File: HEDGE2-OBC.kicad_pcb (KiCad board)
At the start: 4 copper layers, 90.2 x 95.9 mm, 55 parts, among them J1 SQT-110-01-L-D, J2 MMBX-S50-0-18, J3 SMA-J-P-X-RA-TH1, U1 OEM719, U2 INA260AIPWR, U3 TCAN1046AVDYYRQ1, U4 INA260AIPWR, U5 TPS543320RPYR

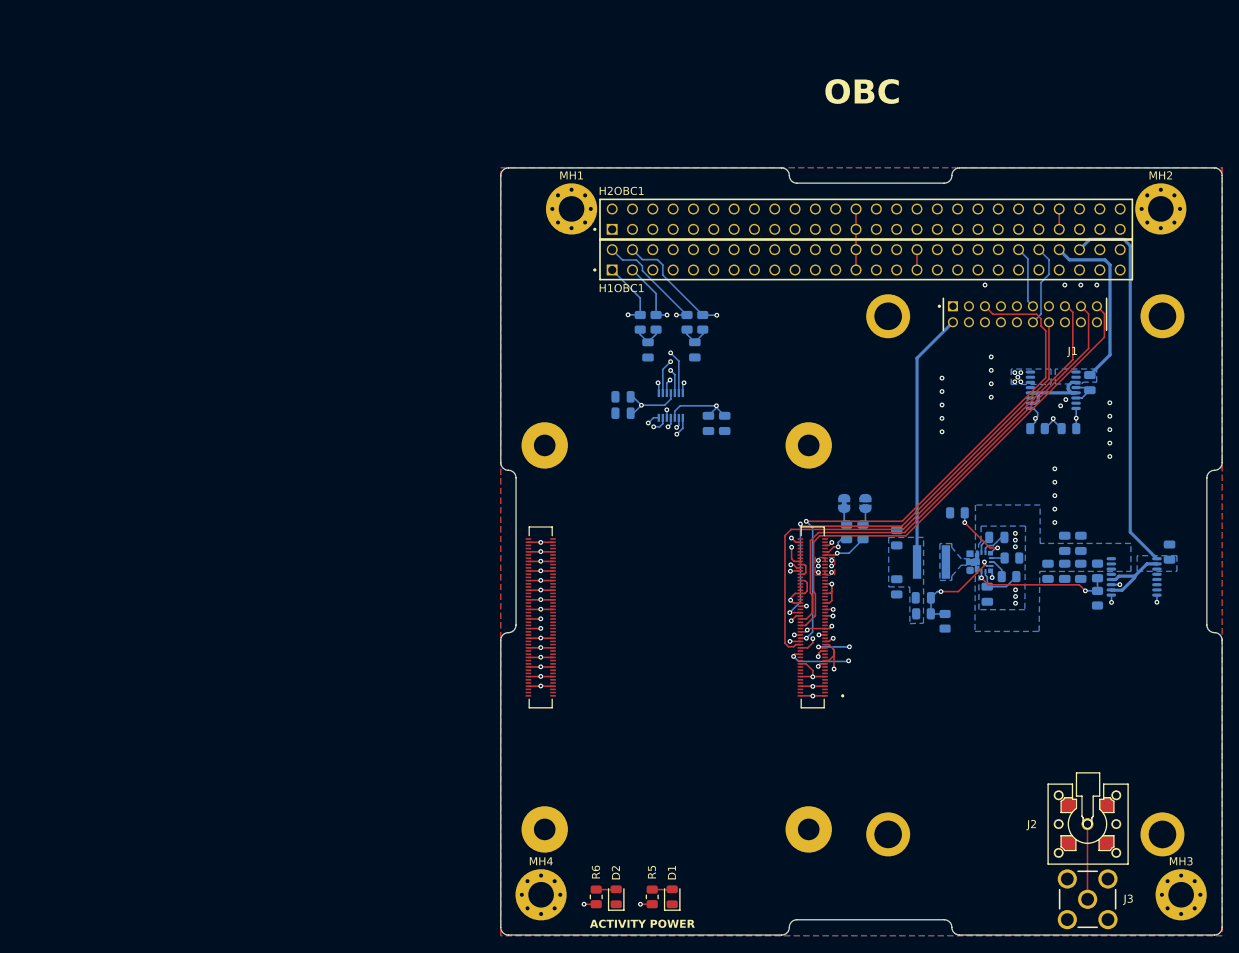
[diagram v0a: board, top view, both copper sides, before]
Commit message: Start new PCB layout for second test article
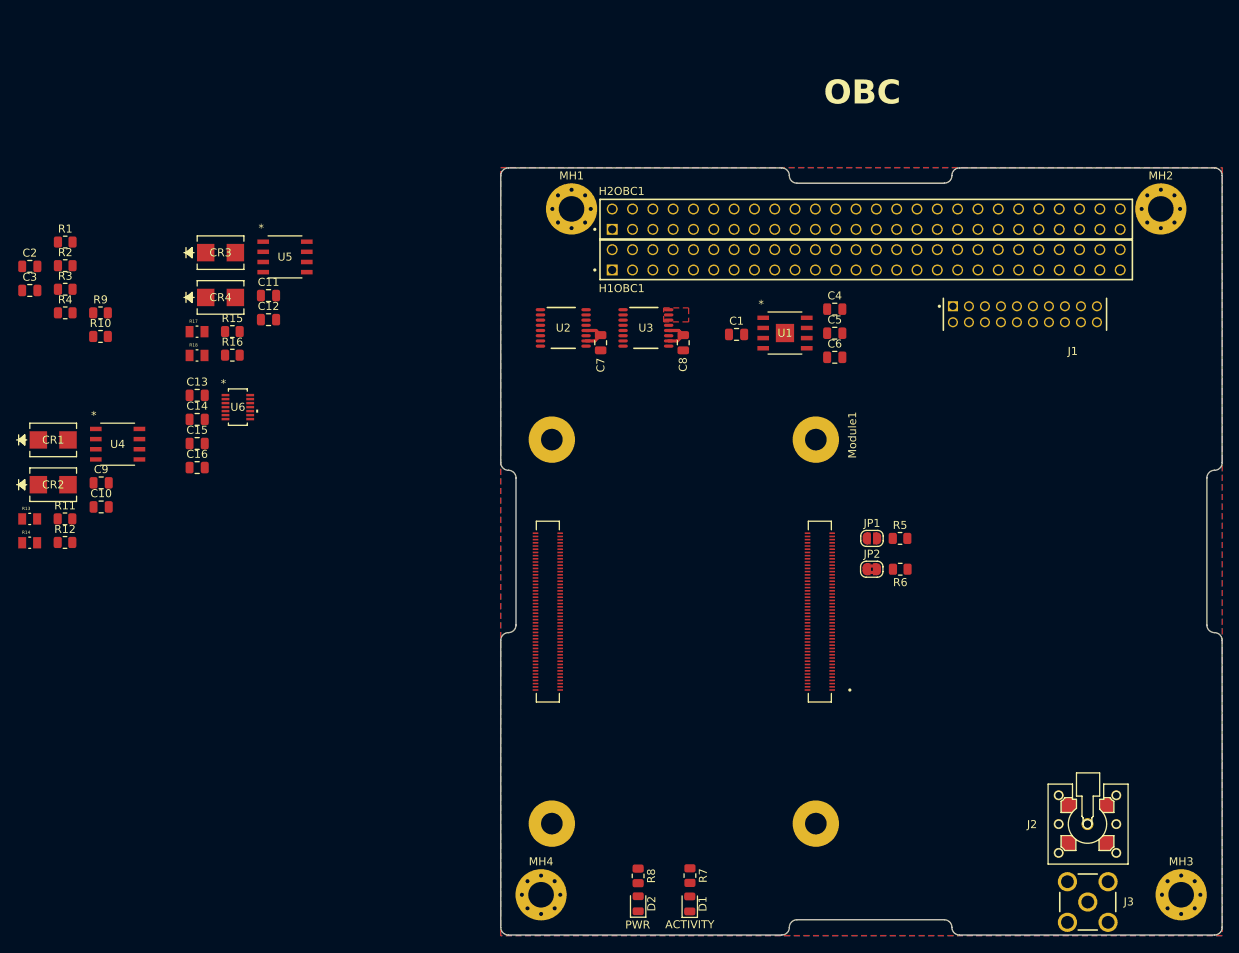
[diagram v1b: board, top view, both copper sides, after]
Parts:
- removed C17, C18: 47u, 10V, 0805, Capacitor_SMD:C_0805_2012Metric
- removed L1: XGL5050-182MEC, XGL5050-182MEC:IND_XGL5050_COC
- added CR1: SMBJ43CA, SMBJ43CA:SMBJSeries_LTF, F.Cu at (108.2, 123.5)
- added CR2: SMBJ43CA, SMBJ43CA:SMBJSeries_LTF, F.Cu at (108.2, 129.1)
- added CR3: SMBJ43CA, SMBJ43CA:SMBJSeries_LTF, F.Cu at (129.1, 100.1)
- added CR4: SMBJ43CA, SMBJ43CA:SMBJSeries_LTF, F.Cu at (129.1, 105.7)
- added R18: CRGP0805F10R, CRGP0805F10R:RESC2012X65N, F.Cu at (126.1, 113.0)
- added U6: TCAN1046AVDYYRQ1, TCAN1046AV:SOT23_DYY_TEX, F.Cu at (131.2, 119.4)
- C1, C5: value 0u1 -> 1u; moved to F.Cu
- C10, C11: value 10u, 25V, 0805 -> 100n; moved to F.Cu
- C12: value 0u1, 50v, 0805 -> 100n; moved to F.Cu
- C13: value 0u1, 50v, 0805 -> 4u7; moved to F.Cu
- C14: value 2u2, 10V, 0805 -> 0u1; moved to F.Cu
- C15: value 0u1, 50V, 0805 -> 4u7; moved to F.Cu
- C16: value 33p -> 0u1; moved to F.Cu
- C2, C8, JP1, R1, R10, R15, R2, R3, R4, R9, U2: moved to F.Cu
- C3: value 0.1u -> 0u1; moved to F.Cu
- C4: value 4u7 -> 10u; moved to F.Cu
- C6: value 4u7 -> 1u; moved to F.Cu
- C7: value 0u1 -> 0.1u; moved to F.Cu
- C9: value 100u, 35V -> 100n; moved to F.Cu
- J1: value SQT-110-01-L-D -> MMBX-S50-0-18
- J2: value MMBX-S50-0-18 -> SQT-110-01-L-D
- JP2: footprint Jumper:SolderJumper-2_P1.3mm_Bridged_RoundedPad1.0x1.5mm -> Jumper:SolderJumper-2_P1.3mm_Bridged2Bar_RoundedPad1.0x1.5mm; moved to F.Cu
- R11: value 16k9 -> 10k; moved to F.Cu
- R12: value 6k04 -> 10k; moved to F.Cu
- R13: value 11k3 -> CRGP0805F10R; footprint Resistor_SMD:R_0805_2012Metric -> CRGP0805F10R:RESC2012X65N; moved to F.Cu
- R14: value 11k8 -> CRGP0805F10R; footprint Resistor_SMD:R_0805_2012Metric -> CRGP0805F10R:RESC2012X65N; moved to F.Cu
- R16: value 4k99 -> 10k; moved to F.Cu
- R17: value 28k -> CRGP0805F10R; footprint Resistor_SMD:R_0805_2012Metric -> CRGP0805F10R:RESC2012X65N; moved to F.Cu
- R5: value 39 -> 1k
- R6: value 45 -> 1k
- R7: value 1k -> 39; moved to F.Cu
- R8: value 1k -> 45; moved to F.Cu
- U1: value OEM719 -> ADP7158ARDZ-3.3-R7; footprint Novatel:OEM719 -> ADP7158ARDZ_3_3_R7:ADP7158ARDZ-3.3-R7_ADI; moved to F.Cu
- U3: value TCAN1046AVDYYRQ1 -> INA260AIPWR; footprint TCAN1046AV:SOT23_DYY_TEX -> INA260AIPWR:PW0016A_L; moved to F.Cu
- U4: value INA260AIPWR -> SN65HVD1782QDRQ1; footprint INA260AIPWR:PW0016A_L -> SN65HVD1782QDRQ1:D8_TEX; moved to F.Cu
- U5: value TPS543320RPYR -> SN65HVD1782QDRQ1; footprint TPS543320RPYR:RPY0014A-MFG -> SN65HVD1782QDRQ1:D8_TEX; moved to F.Cu
- moved C3 146.2 mm to (105.2, 104.9), turned to 0 degrees
- moved R12 129.3 mm to (109.6, 136.4), turned to 0 degrees
- moved R11 129.2 mm to (109.6, 133.4), turned to 0 degrees
- moved R13 122.9 mm to (105.2, 133.4)
- moved R10 121.6 mm to (114.1, 110.6), turned to 0 degrees
- moved C10 120.7 mm to (114.2, 131.9), turned to 0 degrees
- moved C9 118.9 mm to (114.2, 128.9), turned to 0 degrees
- moved R9 118.0 mm to (114.1, 107.7)
- moved U4 117.1 mm to (116.2, 124.1), turned to 0 degrees
- moved R14 116.0 mm to (105.2, 136.4), turned to 0 degrees
- moved C13 110.0 mm to (126.2, 118.0), turned to 0 degrees
- moved C11 107.2 mm to (135.1, 105.5), turned to 0 degrees
- moved C12 105.3 mm to (135.1, 108.5), turned to 0 degrees
- moved R15 101.8 mm to (130.6, 110.0), turned to 0 degrees
- moved C14 101.2 mm to (126.2, 121.0), turned to 0 degrees
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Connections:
- net /OBC/5V_PERM renamed /5V_PERM
- net /OBC/BATT renamed /BATT
- net /OBC/DS_A renamed /DS_A
- net /OBC/DS_B renamed /DS_B
- net /OBC/DS_C renamed /DS_C
- net /OBC/ENA_PWR_1 renamed /ENA_PWR_1
- net /OBC/ENA_PWR_2 renamed /ENA_PWR_2
- net /OBC/ENA_PWR_3 renamed /ENA_PWR_3
- net /OBC/ENA_PWR_4 renamed /ENA_PWR_4
- net /OBC/ENA_PWR_5 renamed /ENA_PWR_5
- net /OBC/ENA_PWR_6 renamed /ENA_PWR_6
- net /OBC/ENA_PWR_7 renamed /ENA_PWR_7
- net /OBC/ENA_PWR_8 renamed /ENA_PWR_8
- net /OBC/PWR_3 renamed /PWR_3
- net /OBC/PWR_4 renamed /PWR_4
- net /OBC/PWR_5 renamed /PWR_5
- net /OBC/PWR_6 renamed /PWR_6
- net /OBC/PWR_7 renamed /PWR_7
- net /OBC/PWR_8 renamed /PWR_8
- net /OBC/RBF_A renamed /RBF_A
- net /OBC/RBF_B renamed /RBF_B
- net /OBC/RBF_C renamed /RBF_C
- net /OBC/UART_A_RX renamed /UART_A_RX
- net /OBC/UART_A_TX renamed /UART_A_TX
- net /OBC/UART_B_RX renamed /UART_B_RX
- net /OBC/UART_B_TX renamed /UART_B_TX
- net /OBC/UART_C_RX renamed /UART_C_RX
- net /OBC/UART_C_TX renamed /UART_C_TX
- C1 pad 1: Net-(C1-Pad1) -> GND
- C1 pad 2: GND -> Net-(U1-BYP)
- C10 pad 1: /OBC/INA260_OEM719/LOAD -> GND
- C10 pad 2: GND -> +5V_CM4
- C11 pad 1: /OBC/INA260_OEM719/LOAD -> GND
- C11 pad 2: GND -> +5V_CM4
- C12 pad 1: /OBC/INA260_OEM719/LOAD -> GND
- C12 pad 2: GND -> +5V_CM4
- C13 pad 1: /OBC/INA260_OEM719/LOAD -> +3V3
- C14 pad 1: Net-(U5-BP5) -> +3V3
- C15 pad 1: Net-(U5-BOOT) -> +5V_CM4
- C15 pad 2: Net-(C15-Pad2) -> GND
- C16 pad 1: +5V_OEM719B -> +5V_CM4
- C16 pad 2: Net-(U5-FB) -> GND
- C3 pad 1: GND -> Net-(C3-Pad1)
- C3 pad 2: +5V_GNSS -> GND
- C4 pad 1: +3V3 -> +5V_OEM719B
- C5 pad 1: +3V3 -> Net-(U1-REF)
- C6 pad 1: +5V_CM4 -> Net-(U1-VREG)
- C7 pad 1: +5V_CM4 -> GND
- C7 pad 2: GND -> +5V_MPU
- C8 pad 2: +5V_MPU -> +5V_GNSS
- C9 pad 1: /OBC/INA260_OEM719/LOAD -> GND
- C9 pad 2: GND -> +5V_CM4
- H1OBC1 pad 01: /OBC/CAN_A_L -> /CAN_A_L
- H1OBC1 pad 02: /OBC/CAN_B_L -> /CAN_B_L
- H1OBC1 pad 03: /OBC/CAN_A_H -> /CAN_A_H
- H1OBC1 pad 04: /OBC/CAN_B_H -> /CAN_B_H
- H1OBC1 pad 22: /OBC/UART_COMM_TX -> /UART_D_TX
- H1OBC1 pad 24: /OBC/UART_COMM_RX -> /UART_D_RX
- H1OBC1 pad 31: /OBC/CHARGE -> unconnected-(H1OBC1-Pad31)
- H1OBC1 pad 32: /OBC/CHARGE -> unconnected-(H1OBC1-Pad32)
- H1OBC1 pad 38: /OBC/UART_DATA_TX -> /UART_E_TX
- H1OBC1 pad 40: /OBC/UART_DATA_RX -> /UART_E_RX
- H1OBC1 pad 42: /OBC/GNSS_TXD1 -> /GNSS_TXD1
- H1OBC1 pad 44: /OBC/GNSS_RXD1 -> /GNSS_RXD1
- J1 pad 01: unconnected-(J1-Pad01) -> (no net)
- J1 pad 02: +5V_OEM719B -> (no net)
- J1 pad 03: unconnected-(J1-Pad03) -> (no net)
- J1 pad 04: unconnected-(J1-Pad04) -> (no net)
- J1 pad 05: /OBC/GNSS_NRESET_IN -> (no net)
- J1 pad 06: unconnected-(J1-Pad06) -> (no net)
- J1 pad 07: unconnected-(J1-Pad07) -> (no net)
- J1 pad 08: unconnected-(J1-Pad08) -> (no net)
- J1 pad 09: unconnected-(J1-Pad09) -> (no net)
- J1 pad 10: GND -> (no net)
- J1 pad 11: /OBC/GNSS_TXD1 -> (no net)
- J1 pad 12: /OBC/GNSS_RXD1 -> (no net)
- J1 pad 13: GND -> (no net)
- J1 pad 14: /OBC/GNSS_TXD2 -> (no net)
- J1 pad 15: /OBC/GNSS_RXD2 -> (no net)
- J1 pad 16: GND -> (no net)
- J1 pad 17: /OBC/GNSS_PV -> (no net)
- J1 pad 18: GND -> (no net)
- J1 pad 19: /OBC/GNSS_PPS -> (no net)
- J1 pad 20: unconnected-(J1-Pad20) -> (no net)
- J2 pad 1: /OBC/RF_GNSS -> (no net)
- J2 pad 2: GND -> (no net)
- J3 pad 1: /OBC/RF_GNSS -> /RF_GNSS
- JP1 pad 1: GND -> Net-(JP1-A)
- JP1 pad 2: Net-(JP1-B) -> GND
- JP2 pad 1: Net-(JP2-A) -> GND
- JP2 pad 2: GND -> Net-(JP2-B)
- Module1 pad 21: /OBC/PI_nLED_Activity -> /PI_nLED_Activity
- Module1 pad 28: /OBC/UART_DATA_RX -> /UART_SCI_B
- Module1 pad 29: /OBC/CAN_A_S -> /CAN_A_S
- Module1 pad 31: /OBC/UART_DATA_TX -> /UART_SCI_A
- Module1 pad 34: /OBC/GNSS_RXD2 -> /GNSS_RXD2
- Module1 pad 35: /OBC/CAN_B_RXD -> /CAN_B_RXD
- Module1 pad 36: /OBC/CAN_B_TXD -> /CAN_B_TXD
- Module1 pad 38: /OBC/GNSS_NRESET_IN -> /GNSS_NRESET_IN
- Module1 pad 39: /OBC/UART_COMM_TX -> /UART_SCI_A
- Module1 pad 40: /OBC/UART_COMM_RX -> /UART_SCI_B
- Module1 pad 45: unconnected-(Module1A-GPIO24-Pad45) -> /UART_SCI_DIR
- Module1 pad 46: /OBC/GNSS_PPS -> /GNSS_PPS
- Module1 pad 47: unconnected-(Module1A-GPIO23-Pad47) -> /UART_COMM_DIR
- Module1 pad 50: /OBC/GNSS_PV -> /GNSS_PV
- Module1 pad 51: /OBC/CAN_A_RXD -> /CAN_A_RXD
- Module1 pad 54: /OBC/GNSS_TXD2 -> /GNSS_TXD2
- Module1 pad 55: /OBC/CAN_A_TXD -> /CAN_A_TXD
- Module1 pad 58: /OBC/CAN_B_S -> /CAN_B_S
- Module1 pad 80: /OBC/SCL0 -> /SCL0
- Module1 pad 82: /OBC/SDA0 -> /SDA0
- Module1 pad 95: /OBC/nPWR_LED -> /nPWR_LED
- R1 pad 1: /OBC/CAN_A_H -> /CAN_A_H
- R1 pad 2: Net-(C1-Pad1) -> Net-(C2-Pad1)
- R10 pad 1: /OBC/SDA0 -> /SDA0
- R11 pad 1: /OBC/INA260_OEM719/LOAD -> +5V_CM4
- R11 pad 2: Net-(U5-EN) -> /UART_SCI_B
- R12 pad 1: Net-(U5-EN) -> /UART_SCI_DIR
- R13 pad 1: Net-(U5-MODE) -> Net-(U4-B)
- R13 pad 2: GND -> /UART_E_TX
- R14 pad 1: Net-(U5-SYNC_FSEL) -> Net-(U4-A)
- R14 pad 2: GND -> /UART_E_RX
- R15 pad 1: Net-(U5-BP5) -> +5V_CM4
- R15 pad 2: Net-(U5-PGOOD) -> /UART_SCI_B
- R16 pad 1: GND -> /UART_COMM_DIR
- R16 pad 2: Net-(U5-FB) -> GND
- R17 pad 1: Net-(U5-FB) -> Net-(U5-B)
- R17 pad 2: +5V_OEM719B -> /UART_D_TX
- R2 pad 1: Net-(C1-Pad1) -> Net-(C2-Pad1)
- R2 pad 2: /OBC/CAN_A_L -> /CAN_A_L
- R3 pad 1: /OBC/CAN_B_H -> /CAN_B_H
- R3 pad 2: Net-(C2-Pad1) -> Net-(C3-Pad1)
- R4 pad 1: Net-(C2-Pad1) -> Net-(C3-Pad1)
- R4 pad 2: /OBC/CAN_B_L -> /CAN_B_L
- R5 pad 1: /OBC/PI_nLED_Activity -> Net-(JP1-A)
- R5 pad 2: Net-(D1-A) -> Net-(Module1A-WiFi_nDisable)
- R6 pad 1: /OBC/nPWR_LED -> Net-(Module1A-BT_nDisable)
- R6 pad 2: Net-(D2-A) -> Net-(JP2-B)
- R7 pad 1: Net-(JP1-B) -> /PI_nLED_Activity
- R7 pad 2: Net-(Module1A-WiFi_nDisable) -> Net-(D1-A)
- R8 pad 1: Net-(Module1A-BT_nDisable) -> /nPWR_LED
- R8 pad 2: Net-(JP2-A) -> Net-(D2-A)
- R9 pad 1: /OBC/SCL0 -> /SCL0
- U2 pad 1: +5V_GNSS -> +5V_MPU
- U2 pad 10: +5V_GNSS -> +5V_MPU
- U2 pad 12: +5V_GNSS -> +5V_MPU
- U2 pad 14: /OBC/INA260_OEM719/LOAD -> +5V_CM4
- U2 pad 15: /OBC/INA260_OEM719/LOAD -> +5V_CM4
- U2 pad 16: /OBC/INA260_OEM719/LOAD -> +5V_CM4
- U2 pad 2: +5V_GNSS -> +5V_MPU
- U2 pad 3: +5V_GNSS -> +5V_MPU
- U2 pad 5: GND -> +5V_MPU
- U2 pad 8: /OBC/SDA0 -> /SDA0
- U2 pad 9: /OBC/SCL0 -> /SCL0
- U3 pad 1: /OBC/CAN_A_TXD -> +5V_GNSS
- U3 pad 10: /OBC/CAN_B_H -> +5V_GNSS
- U3 pad 11: +5V_CM4 -> GND
- U3 pad 12: /OBC/CAN_A_L -> +5V_GNSS
- U3 pad 13: /OBC/CAN_A_H -> unconnected-(U3-NC-Pad13)
- U3 pad 14: /OBC/CAN_A_S -> +5V_OEM719B
- U3 pad 2: GND -> +5V_GNSS
- U3 pad 3: +3V3 -> +5V_GNSS
- U3 pad 4: /OBC/CAN_A_RXD -> GND
- U3 pad 6: /OBC/CAN_B_TXD -> GND
- U3 pad 7: /OBC/CAN_B_RXD -> unconnected-(U3-ALERT-Pad7)
- U3 pad 8: /OBC/CAN_B_S -> /SDA0
- U3 pad 9: /OBC/CAN_B_L -> /SCL0
- U4 pad 1: +5V_MPU -> /UART_SCI_B
- U4 pad 2: +5V_MPU -> /UART_SCI_DIR
- U4 pad 3: +5V_MPU -> /UART_SCI_DIR
- U4 pad 4: GND -> /UART_SCI_A
- U4 pad 5: +5V_MPU -> GND
- U4 pad 6: GND -> Net-(U4-A)
- U4 pad 7: unconnected-(U4-ALERT-Pad7) -> Net-(U4-B)
- U4 pad 8: /OBC/SDA0 -> +5V_CM4
- U5 pad 1: Net-(U5-SYNC_FSEL) -> /UART_SCI_B
- U5 pad 2: Net-(U5-MODE) -> /UART_COMM_DIR
- U5 pad 3: Net-(U5-PGOOD) -> /UART_COMM_DIR
- U5 pad 4: Net-(U5-FB) -> /UART_SCI_A
- U5 pad 6: Net-(U5-BP5) -> Net-(U5-A)
- U5 pad 7: Net-(U5-EN) -> Net-(U5-B)
- U5 pad 8: /OBC/INA260_OEM719/LOAD -> +5V_CM4
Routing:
- net GND: track 92.9 -> 0.00 mm, vias 62 -> 0
- net /OBC/SDA0: track 81.3 -> 0.00 mm, vias 3 -> 0
- net /OBC/SCL0: track 75.9 -> 0.00 mm, vias 3 -> 0
- net /OBC/GNSS_NRESET_IN: track 68.7 -> 0.00 mm, vias 2 -> 0
- net /OBC/GNSS_RXD2: track 68.0 -> 0.00 mm
- net /OBC/nPWR_LED: track 67.5 -> 0.00 mm, vias 2 -> 0
- net /OBC/UART_DATA_RX: track 67.4 -> 0.00 mm, vias 2 -> 0
- net /OBC/UART_DATA_TX: track 63.0 -> 0.00 mm, vias 2 -> 0
- net /OBC/GNSS_PPS: track 62.9 -> 0.00 mm
- net /OBC/GNSS_PV: track 61.3 -> 0.00 mm
- net /OBC/UART_COMM_TX: track 59.2 -> 0.00 mm, vias 1 -> 0
- net /OBC/GNSS_TXD2: track 58.8 -> 0.00 mm, vias 2 -> 0
- net +5V_GNSS: track 58.0 -> 4.19 mm
- net /OBC/UART_COMM_RX: track 52.2 -> 0.00 mm, vias 1 -> 0
- net /OBC/CAN_B_RXD: track 47.9 -> 0.00 mm, vias 2 -> 0
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- added copper zone on F.Cu, net +5V_OEM719B
- removed copper zone on B.Cu, net +5V_CM4
- removed copper zone on F.Cu, net +5V_CM4
- removed copper zone on B.Cu, net +5V_GNSS
- removed copper zone on B.Cu, net +5V_MPU
- removed copper zone on B.Cu, net +5V_OEM719B
- removed copper zone on B.Cu, net /OBC/INA260_OEM719/LOAD
- removed copper zone on B.Cu, net Net-(L1-Pad1)
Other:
- board text added: "PWR"
- board text removed: "POWER"

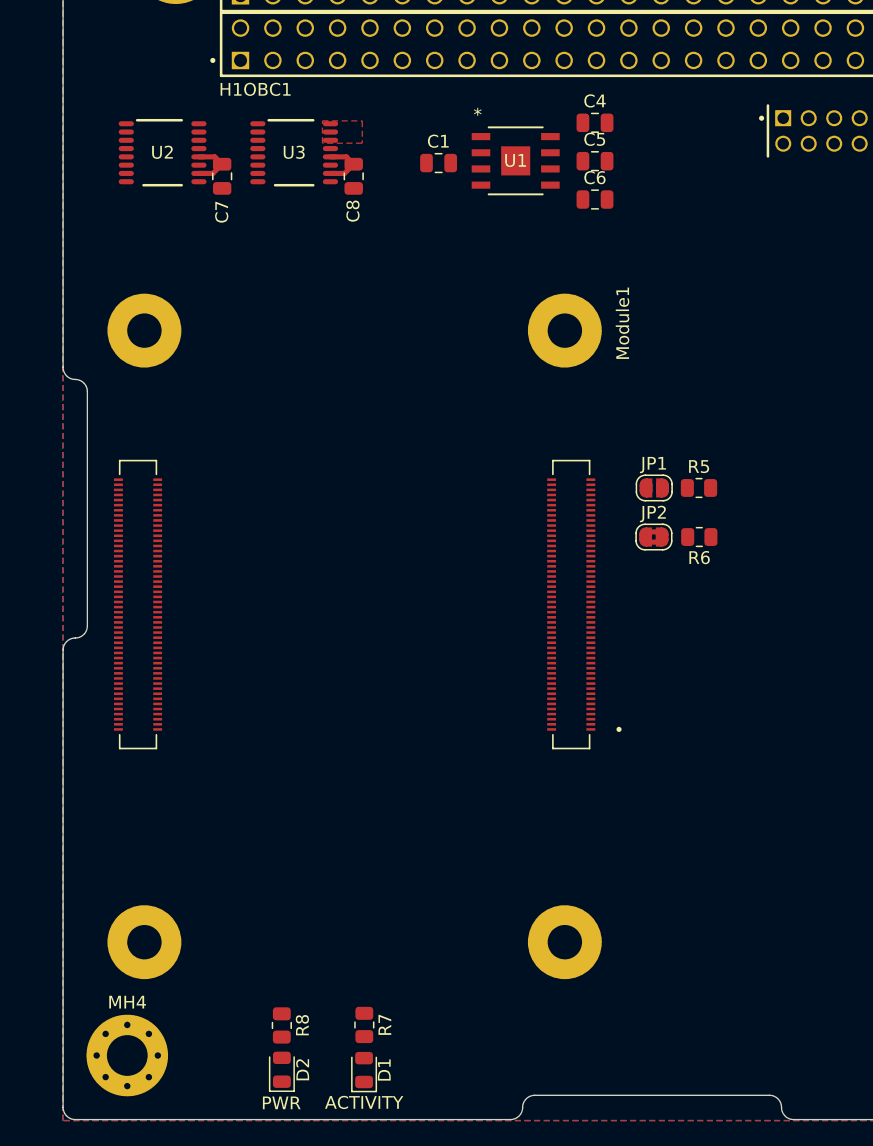
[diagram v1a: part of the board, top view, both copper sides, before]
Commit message: Add power zones on In1 and In2
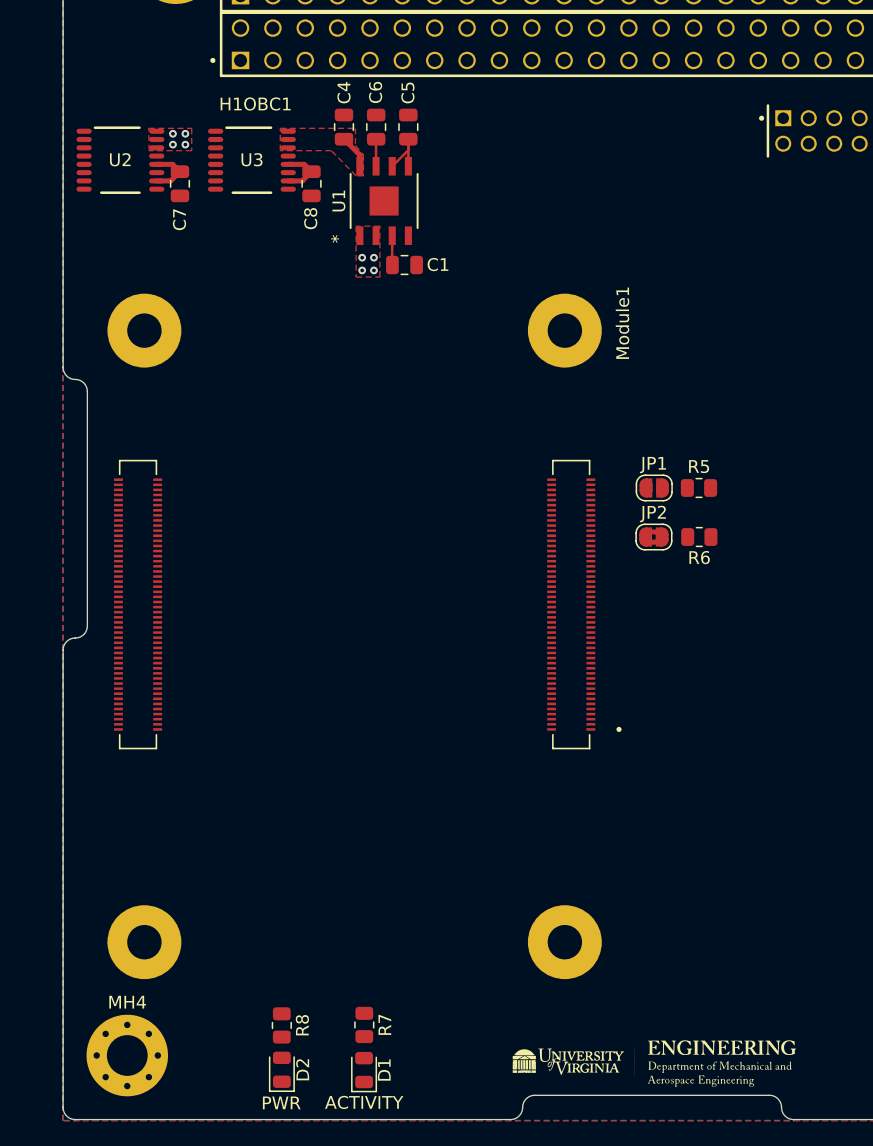
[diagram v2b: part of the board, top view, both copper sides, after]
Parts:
- added G***: LOGO, HEDGElogo:HEDGE-logo, F.Cu at (210.5, 181.0)
- moved C4 19.7 mm to (186.2, 107.5), turned to 90 degrees
- moved C6 18.1 mm to (188.7, 107.5), turned to 90 degrees
- moved C5 14.9 mm to (191.2, 107.5), turned to 90 degrees
- moved U1 10.8 mm to (189.3, 113.3), turned to 90 degrees
- moved C1 8.44 mm to (190.9, 118.3), turned to 180 degrees
- moved U2 3.36 mm to (168.6, 110.1)
- moved U3 3.36 mm to (178.9, 110.1)
- moved C7 3.36 mm to (173.3, 112.0)
- moved C8 3.36 mm to (183.6, 112.0)
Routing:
- net Net-(U1-REF): track 0.00 -> 4.78 mm
- net +5V_OEM719B: track 0.00 -> 2.64 mm
- net Net-(U1-BYP): track 0.00 -> 2.31 mm
- net Net-(U1-VREG): track 0.00 -> 2.13 mm
- net +5V_CM4: vias 0 -> 4
- net +3V3_OEM719B: vias 0 -> 4
- added copper zone on F.Cu, net +3V3_OEM719B
- added copper zone on In1.Cu, net +3V3_OEM719B
- added copper zone on F.Cu, net +5V_CM4
- removed copper zone on In1.Cu, net +3V3
